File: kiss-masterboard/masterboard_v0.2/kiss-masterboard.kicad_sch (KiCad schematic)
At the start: 26 parts, among them J1 Cubebatt_host, J2 Conn_01x02, J3 Conn_01x02, J4 Conn_01x02, J5 Conn_01x02, J6 Conn_01x02, J7 Conn_01x02

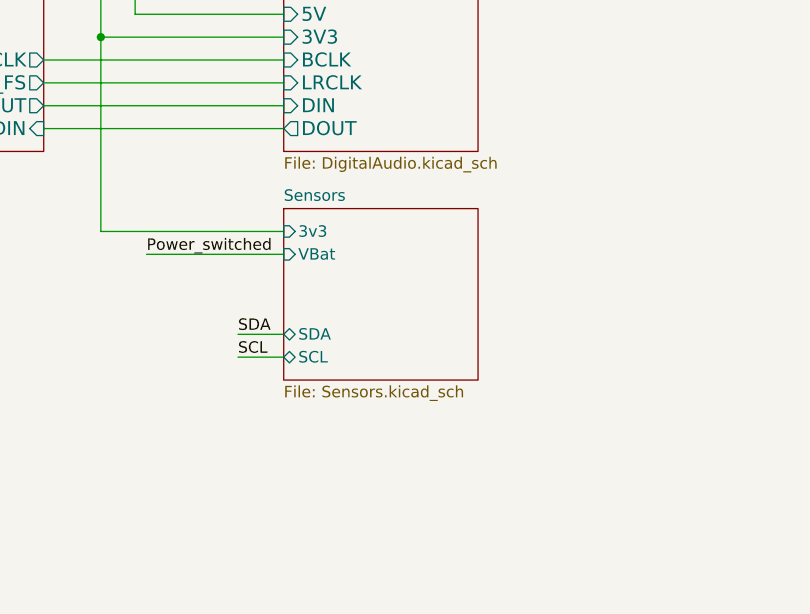
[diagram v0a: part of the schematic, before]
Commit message: replaced symbosl with standart symbols and reduced DRC errorsMAX98357A and TLV75709PDBV symbols
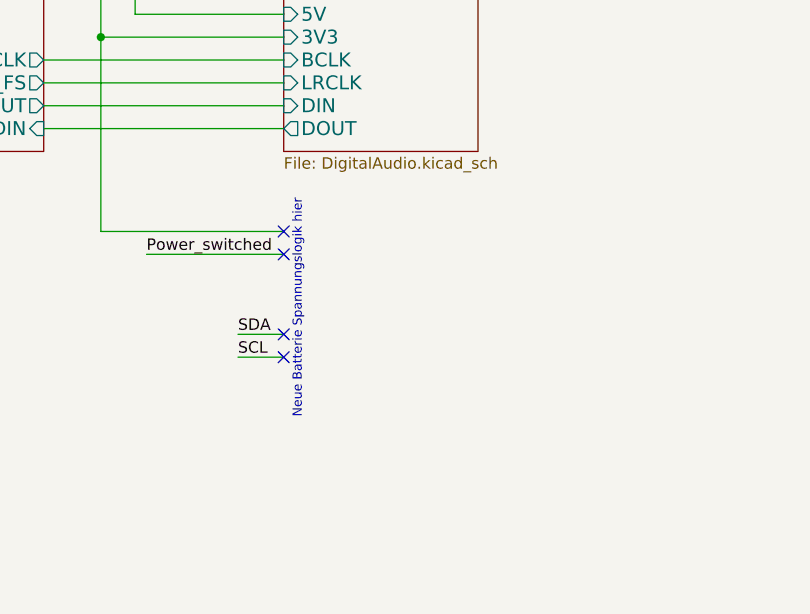
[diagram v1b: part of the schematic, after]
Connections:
- no-connect marks 1 -> 5
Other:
- removed sheet Sensors
- note added: "Neue Batterie Spannungslogik hier"
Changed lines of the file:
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@@
 		(comment 4 "License: CC-BY-SA V4.0")
 	)
+	(text "Neue Batterie Spannungslogik hier"
+		(exclude_from_sim no)
+		(at 128.524 134.366 90)
+		(effects
+			(font
+				(size 1.016 1.016)
+			)
+		)
+	)
 	(text "TODO Route to Raspi?"
 		(exclude_from_sim no)
@@
 	)
 	(no_connect
+		(at 127 125.73)
+	)
+	(no_connect
+		(at 127 137.16)
+	)
+	(no_connect
 		(at 152.4 43.18)
 	)
+	(no_connect
+		(at 127 128.27)
+	)
+	(no_connect
+		(at 127 139.7)
+	)
 	(wire
 		(pts
@@
 				)
 			)
-		)
-	)
-	(sheet
-		(at 127 123.19)
-		(size 21.59 19.05)
-		(exclude_from_sim no)
-		(in_bom yes)
-		(on_board yes)
-		(dnp no)
-		(fields_autoplaced yes)
-		(stroke
-			(width 0)
-			(type solid)
-		)
-		(fill
-			(color 0 0 0 0)
-		)
-		(property "Sheetname" "Sensors"
-			(at 127 122.4784 0)
-			(show_name no)
-			(do_not_autoplace no)
-			(effects
-				(font
-					(size 1.27 1.27)
-				)
-				(justify left bottom)
-			)
-		)
-		(property "Sheetfile" "Sensors.kicad_sch"
-			(at 127 142.8246 0)
-			(show_name no)
-			(do_not_autoplace no)
-			(effects
-				(font
-					(size 1.27 1.27)
-				)
-				(justify left top)
-			)
-		)
-		(pin "SDA" bidirectional
-			(at 127 137.16 180)
-			(effects
-				(font
-					(size 1.27 1.27)
-				)
-				(justify left)
-			)
-		)
-		(pin "SCL" bidirectional
-			(at 127 139.7 180)
-			(effects
-				(font
-					(size 1.27 1.27)
-				)
-				(justify left)
-			)
-		)
-		(pin "3v3" input
-			(at 127 125.73 180)
-			(effects
-				(font
-					(size 1.27 1.27)
-				)
-				(justify left)
-			)
-		)
-		(pin "VBat" input
-			(at 127 128.27 180)
-			(effects
-				(font
-					(size 1.27 1.27)
-				)
-				(justify left)
-			)
-		)
-		(instances
-			(project "kiss-masterboard"
-				(path "/7506bdf8-b028-4bb6-b0dc-a13e261cf434"
-					(page "7")
-				)
-			)

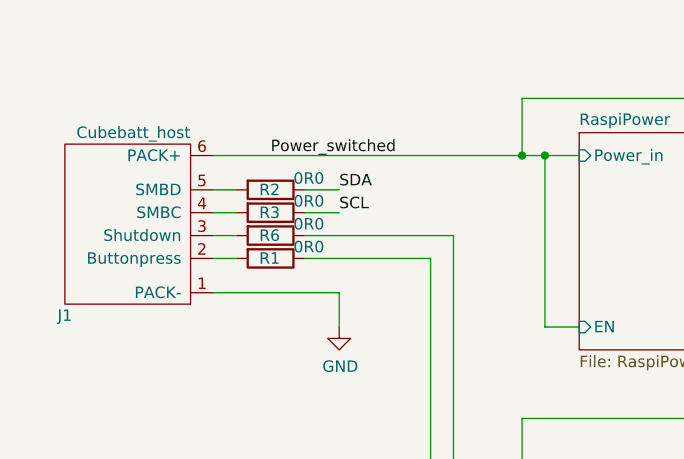
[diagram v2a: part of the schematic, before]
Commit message: Adjust to new batterypack,
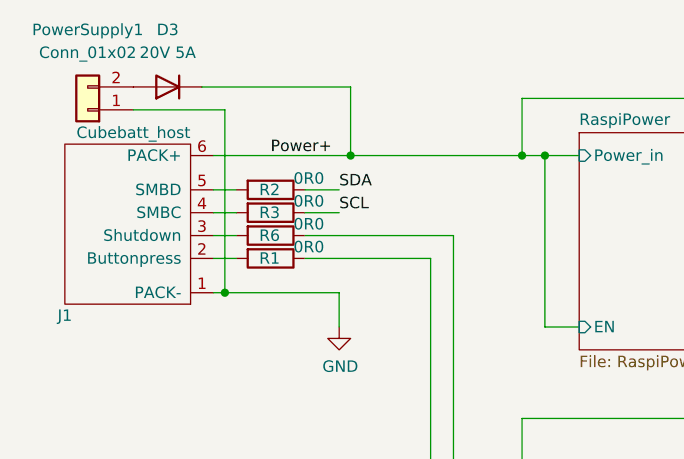
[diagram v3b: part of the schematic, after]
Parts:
- added D3: 20V 5A, Diode_SMD:D_SMA, symbol Device:D
- added PowerSupply1: Conn_01x02, Connector_AMASS:AMASS_XT30PW-F_1x02_P2.50mm_Horizontal, symbol Connector_Generic:Conn_01x02
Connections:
- net GND: now also PowerSupply1.1 (Pin_1)
- net Power_switched: no longer J1.6 (PACK+)
- new net: D3.2 (A), PowerSupply1.2 (Pin_2)
- new net Power+: D3.1 (K), J1.6 (PACK+)

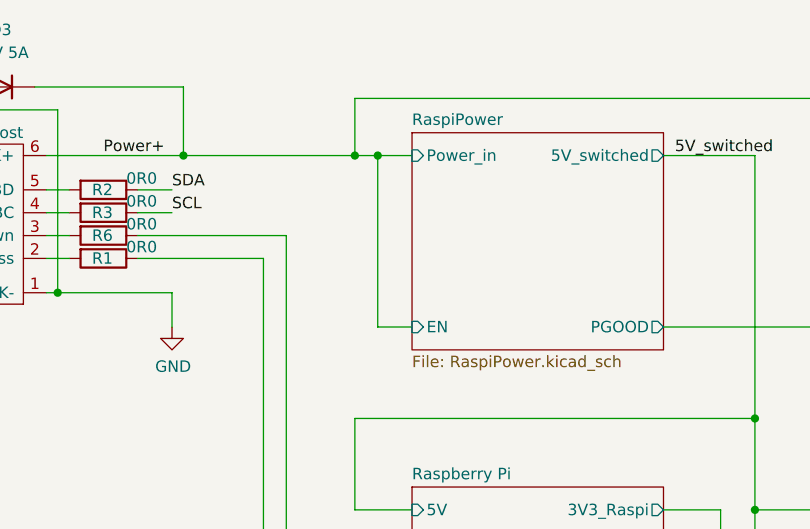
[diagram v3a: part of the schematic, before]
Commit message: Replaced TPS54327 with TPS56339DDC and adjusted the schematic layout accordingly.
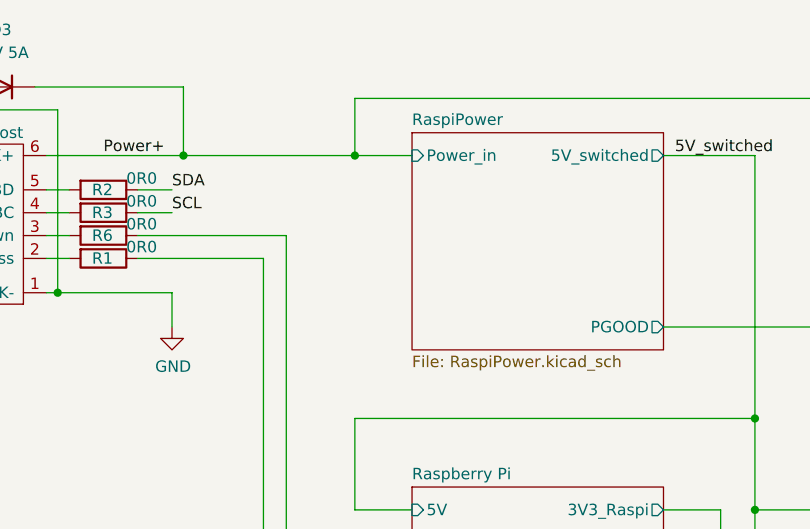
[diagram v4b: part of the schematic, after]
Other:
- sheet RaspiPower ports: added none; removed EN
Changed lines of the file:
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@@
 	)
 	(junction
-		(at 68.58 24.13)
-		(diameter 0)
-		(color 0 0 0 0)
-	)
-	(junction
 		(at 33.02 39.37)
 		(diameter 0)
@@
 	(wire
 		(pts
-			(xy 68.58 24.13) (xy 68.58 43.18)
-		)
-		(stroke
-			(width 0)
-			(type default)
-		)
-	)
-	(wire
-		(pts
 			(xy 58.42 33.02) (xy 58.42 71.12)
 		)
@@
 	(wire
 		(pts
-			(xy 68.58 24.13) (xy 72.39 24.13)
+			(xy 66.04 24.13) (xy 72.39 24.13)
 		)
 		(stroke
@@
 	(wire
 		(pts
-			(xy 68.58 43.18) (xy 72.39 43.18)
-		)
-		(stroke
-			(width 0)
-			(type default)
-		)
-	)
-	(wire
-		(pts
 			(xy 55.88 35.56) (xy 55.88 68.58)
 		)
@@
 	(wire
 		(pts
-			(xy 66.04 24.13) (xy 68.58 24.13)
-		)
-		(stroke
-			(width 0)
-			(type default)
-		)
-	)
-	(wire
-		(pts
 			(xy 256.54 57.15) (xy 251.46 57.15)
 		)
@@
 			)
 		)
-		(pin "EN" input
-			(at 72.39 43.18 180)
-			(effects
-				(font
-					(size 1.27 1.27)
-				)
-				(justify left)
-			)
-		)

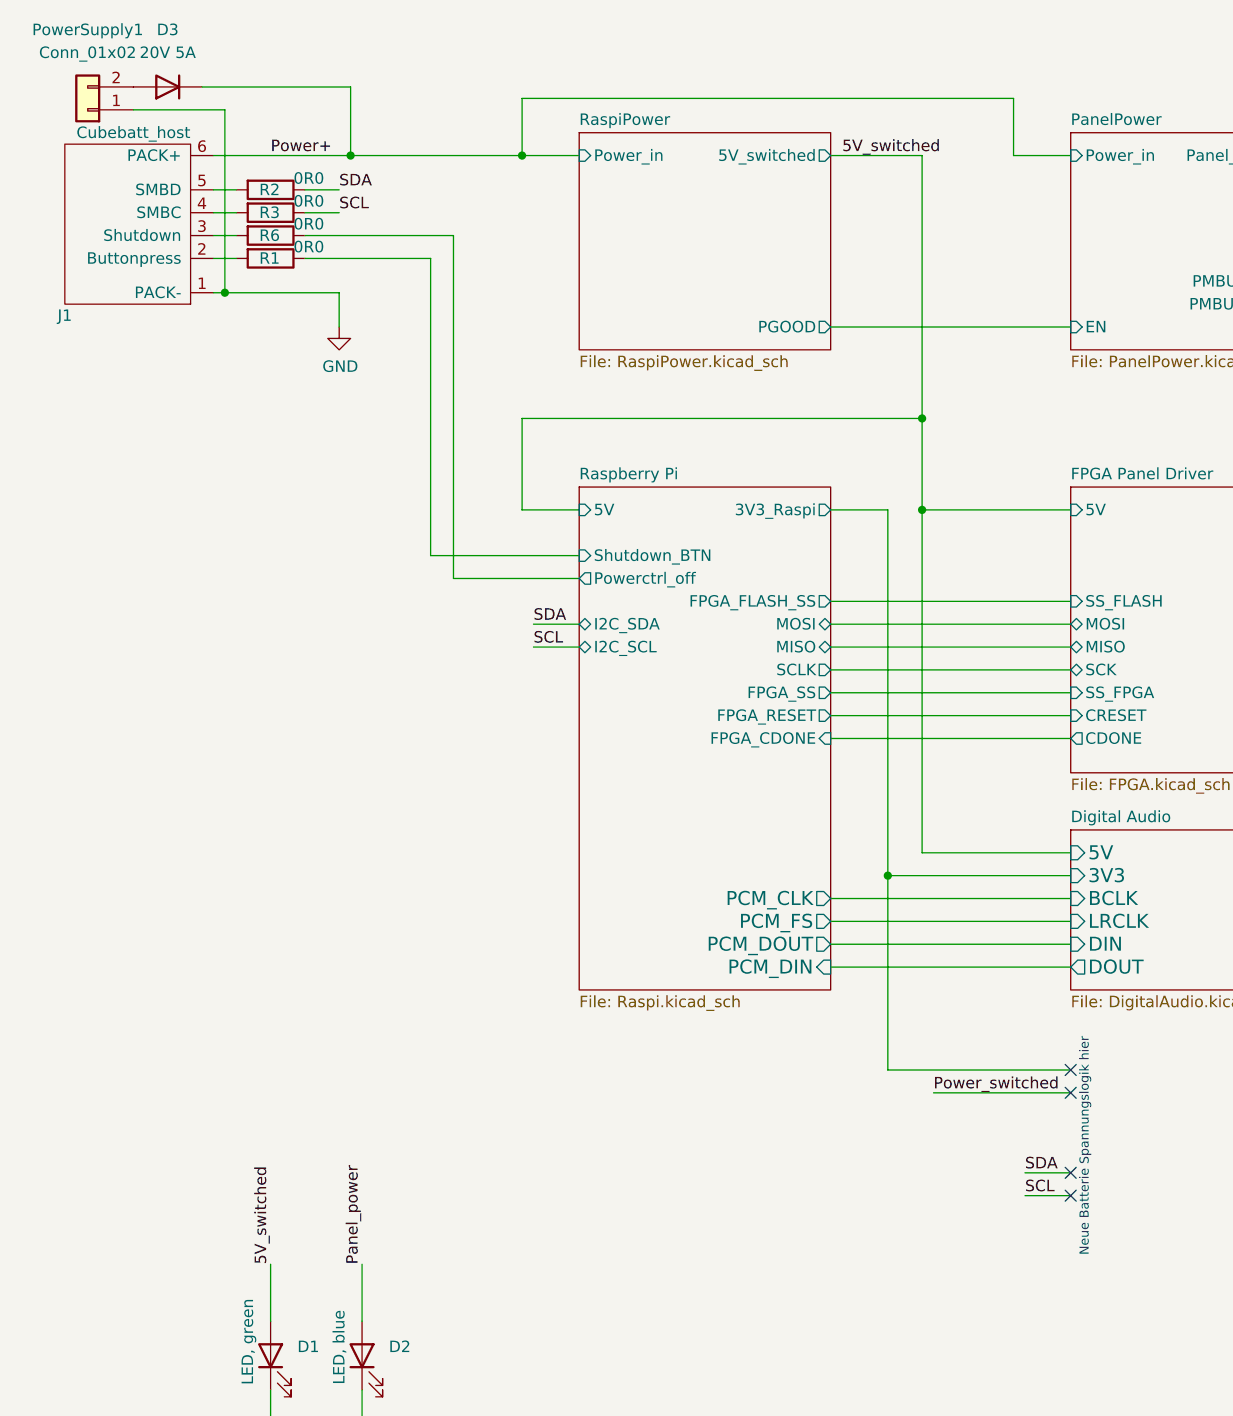
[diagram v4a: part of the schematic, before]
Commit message: Add extension header
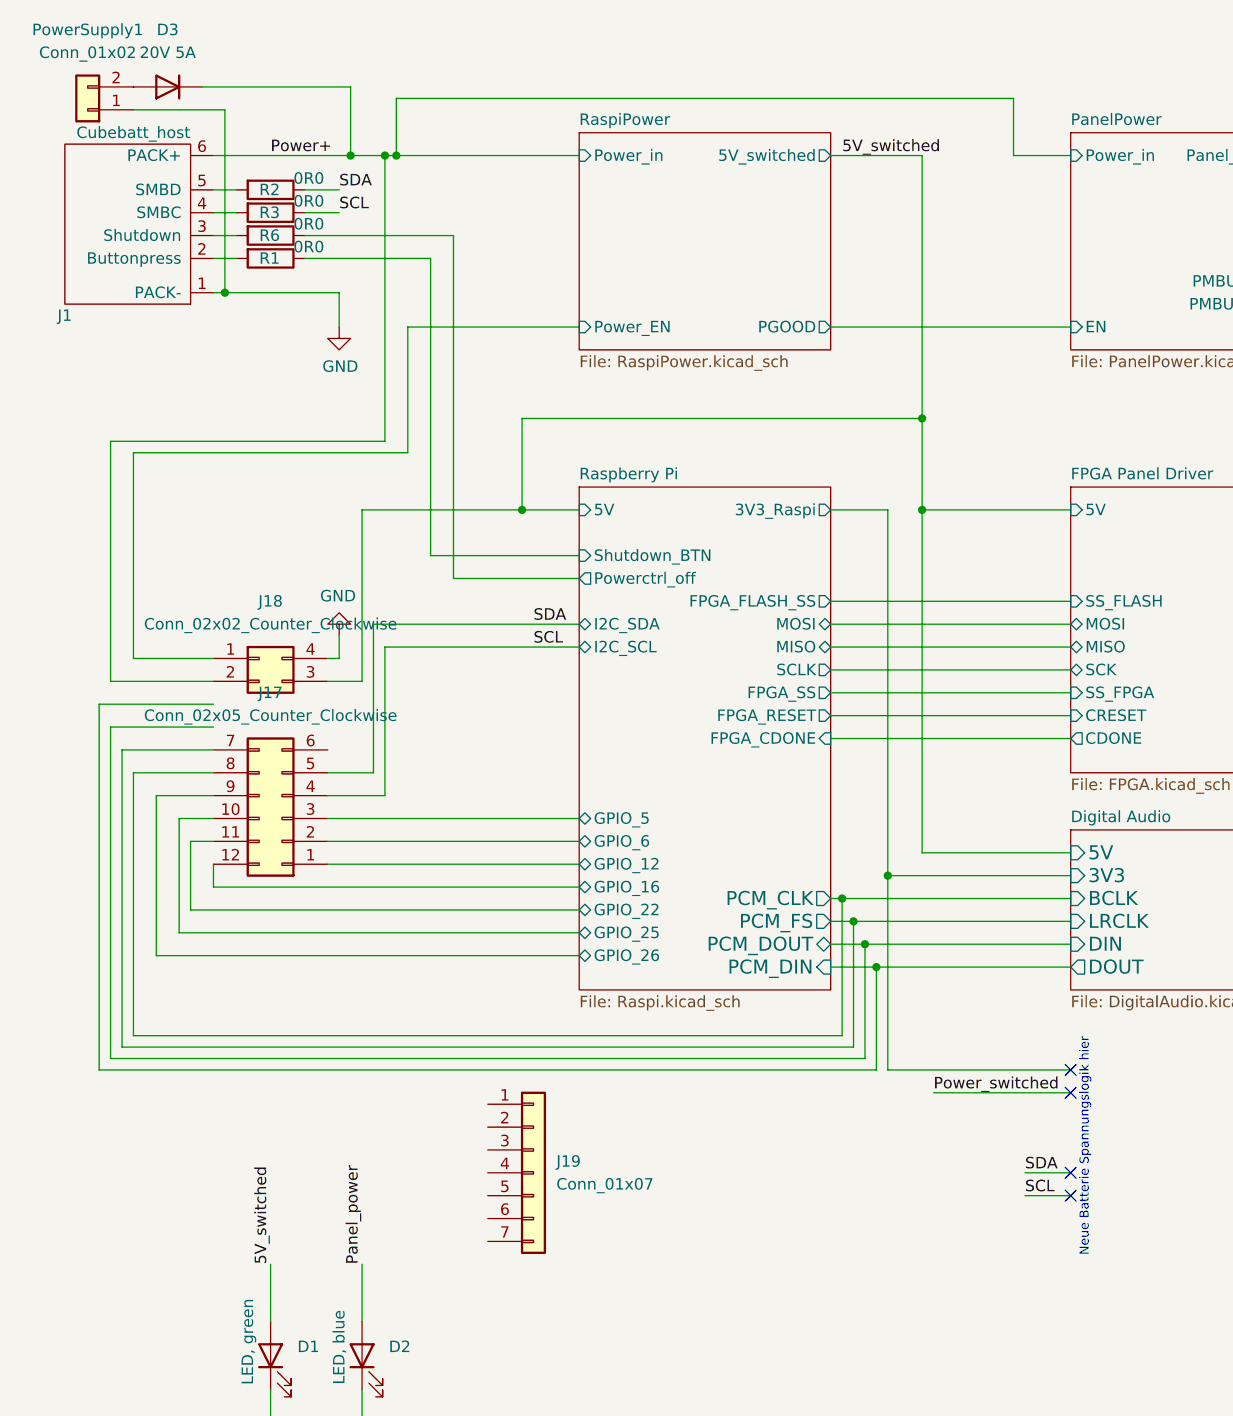
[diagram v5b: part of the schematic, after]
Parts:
- added J17: Conn_02x05_Counter_Clockwise, Connector_PinSocket_2.54mm:PinSocket_2x06_P2.54mm_Vertical_SMD, symbol Connector_Generic:Conn_02x06_Counter_Clockwise
- added J18: Conn_02x02_Counter_Clockwise, Connector_PinSocket_2.54mm:PinSocket_2x02_P2.54mm_Vertical_SMD, symbol Connector_Generic:Conn_02x02_Counter_Clockwise
- added J19: Conn_01x07, symbol Connector_Generic:Conn_01x07
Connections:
- net 5V_switched: now also J18.3 (Pin_3)
- net Digital Audio/BCLK: now also J17.8 (Pin_8)
- net Digital Audio/LRCLK: now also J17.7 (Pin_7)
- net GND: now also J18.4 (Pin_4)
- net Power+: now also J18.2 (Pin_2)
- net SCL: now also J17.4 (Pin_4)
- net SDA: now also J17.5 (Pin_5)
- new net Raspberry Pi/GPIO_12: J17.1 (Pin_1)
- new net Raspberry Pi/GPIO_16: J17.12 (Pin_12)
- new net Raspberry Pi/GPIO_22: J17.11 (Pin_11)
- new net Raspberry Pi/GPIO_25: J17.10 (Pin_10)
- new net Raspberry Pi/GPIO_26: J17.9 (Pin_9)
- new net Raspberry Pi/GPIO_5: J17.3 (Pin_3)
- new net Raspberry Pi/GPIO_6: J17.2 (Pin_2)
- new net RaspiPower/Power_EN: J18.1 (Pin_1)
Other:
- sheet Raspberry Pi ports: added GPIO_12, GPIO_16, GPIO_22, GPIO_25, GPIO_26, GPIO_5, GPIO_6; removed none
- sheet RaspiPower ports: added Power_EN; removed none
